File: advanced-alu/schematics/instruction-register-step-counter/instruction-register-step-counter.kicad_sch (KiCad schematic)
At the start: 17 parts, among them SW1 SW_SPST, U1 74LS32, U2 74LS04, U3 74HCT238, U4 74LS161, U5 74LS173, U6 74LS74, U7 74LS173, U8 74LS08

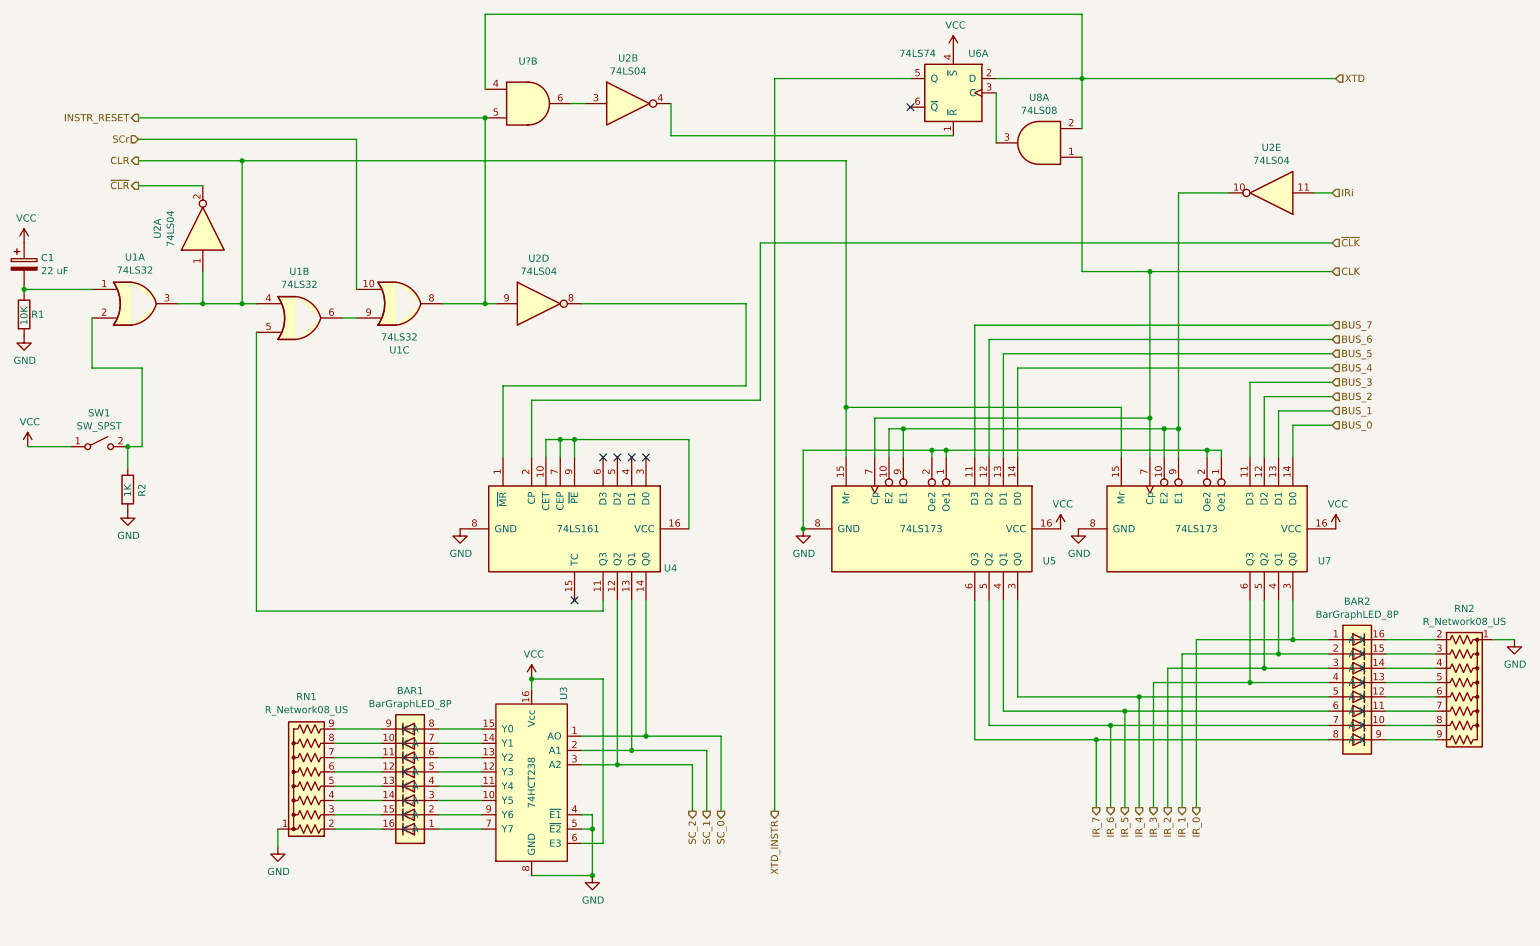
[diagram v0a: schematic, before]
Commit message: fixed STD and step counter resent logic
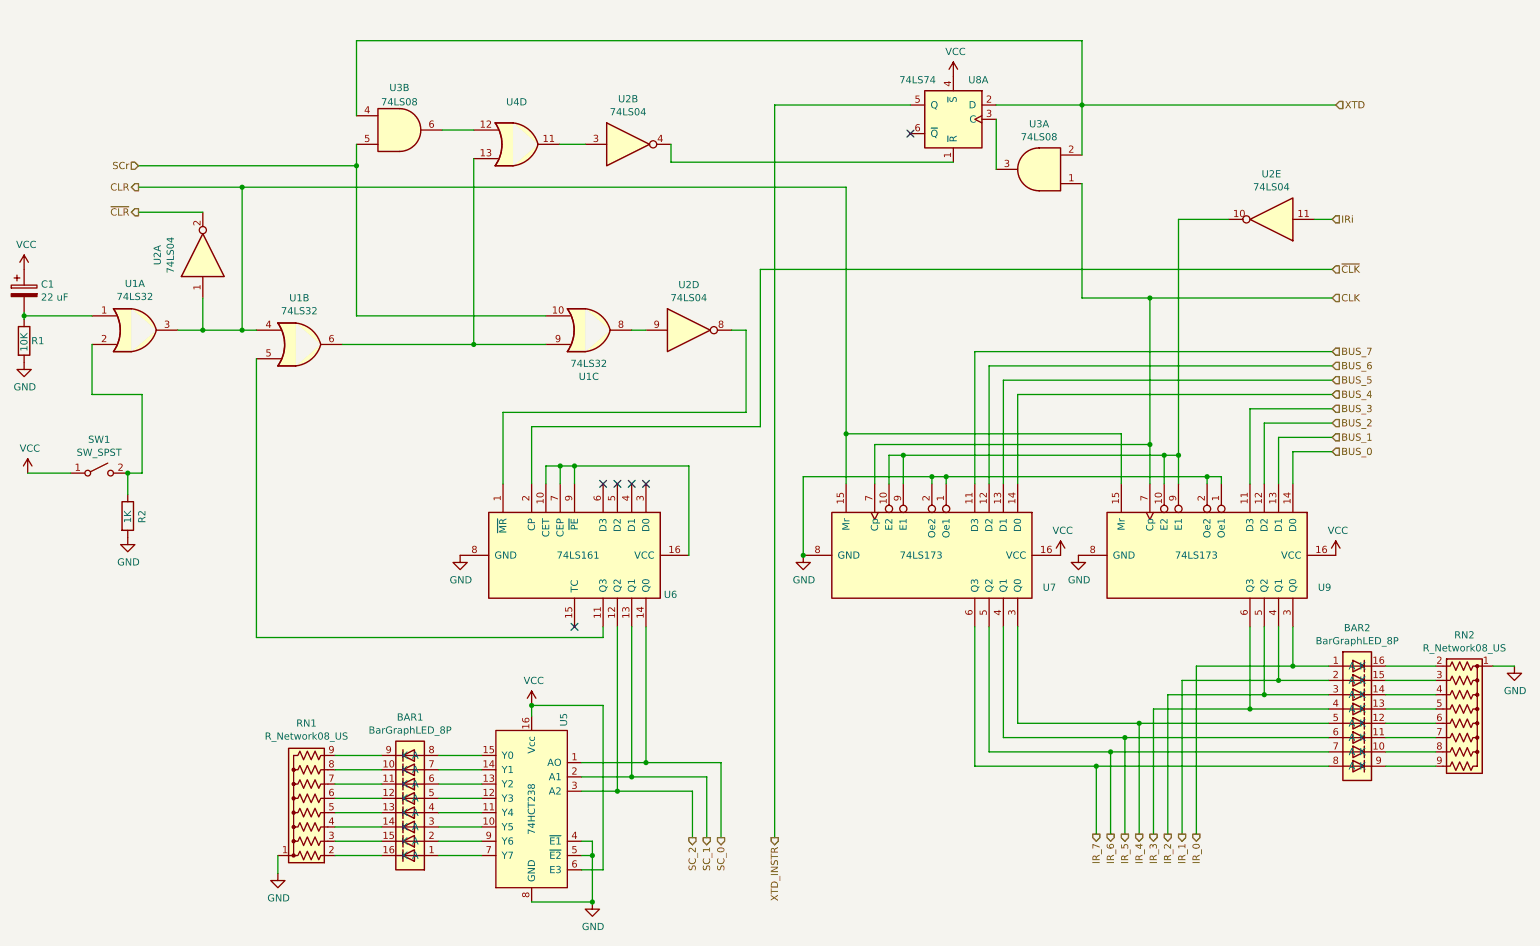
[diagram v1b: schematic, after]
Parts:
- added U4: (no value), symbol 74xx:74LS32
- U3: renamed from U?; value (none) -> 74LS08
- renumbered U8 to U3, U3 to U5, U4 to U6, U5 to U7, U6 to U8, U7 to U9
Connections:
- net SCr: now also U3.5
- net at U1.6, U1.9: now also U4.13
- net at U2.3: now also U4.11; no longer U3.6
- net INSTR_RESET: no longer names the net of U1.8, U2.9
- net INSTR_RESET: no longer U3.5
- new net: U3.6, U4.12
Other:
- moved on the sheet: BAR1, BAR2, C1, R1, R2, RN1, RN2, SW1, U1A, U1B, U1C, U2A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

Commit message: changed how XTD works
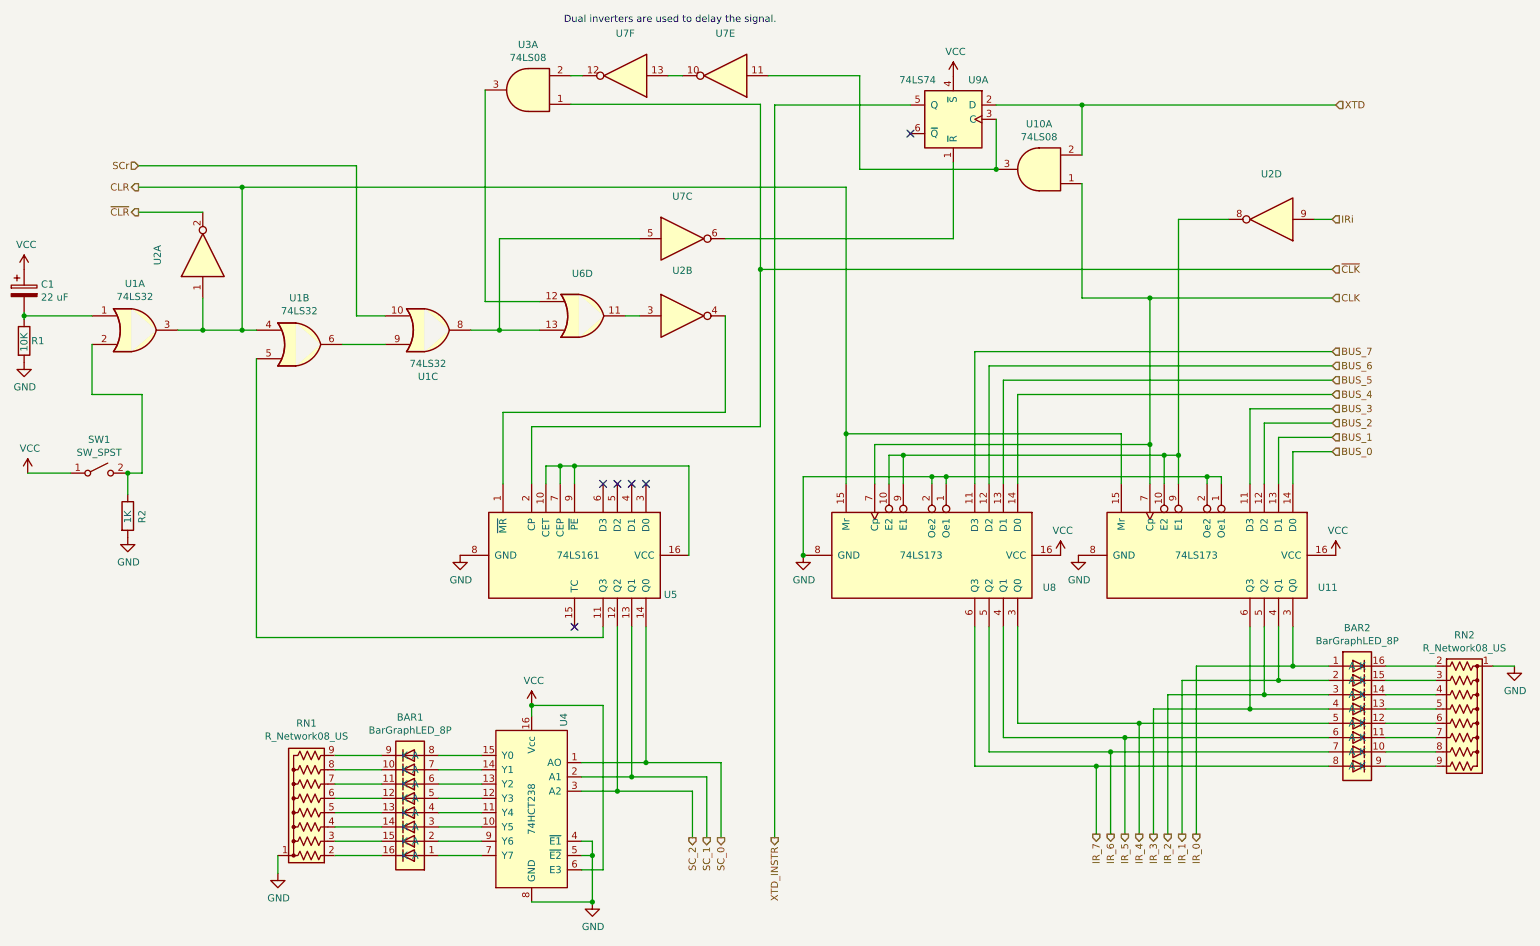
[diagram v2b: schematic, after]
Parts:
- removed unit 2 of U2
- removed unit 2 of U3
- removed U4: (no value), symbol 74xx:74LS32
- added U3: 74LS08, symbol 74xx:74LS08
- added U6: (no value), symbol 74xx:74LS32
- added U7: (no value), symbol 74xx:74LS04
- U2: value 74LS04 -> (none)
- renumbered U3 to U10, U9 to U11, U5 to U4, U6 to U5, U7 to U8, U8 to U9
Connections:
- net IRi: now also U2.9; no longer U2.11
- net ~{CLK}: now also U3.1
- net at U5.1 (~{MR}): now also U2.4; no longer U2.8
- net at U9.1 (~{R}): now also U7.6
- net at U1.8: now also U6.13, U7.5; no longer U2.9
- net at U11.10 (E2), U11.9 (E1), U8.10 (E2)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: now also U2.8; no longer U2.10
- net at U10.3, U9.3 (C): now also U7.11
- new net: U2.3, U6.11
- new net: U3.2, U7.12
- new net: U7.10, U7.13
- new net: U3.3, U6.12
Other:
- note added: "Dual inverters are used to delay the signal."
- moved on the sheet: U1C, U2B

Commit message: updated unit selection
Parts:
- U3: value 74LS08 -> (none)
- U6: value (none) -> 74LS32
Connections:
- net ~{CLK}: now also U3.9; no longer U3.1
- net at U5.1 (~{MR}): now also U2.6; no longer U2.4
- net at U1.8, U6.13: now also U7.9; no longer U7.5
- net at U6.11: now also U2.5; no longer U2.3
- net at U9.1 (~{R}): now also U7.8; no longer U7.6
- net at U10.3, U9.3 (C): now also U7.13; no longer U7.11
- net at U6.12: now also U3.8; no longer U3.3
- new net: U3.10, U7.10
- new net: U7.11, U7.12
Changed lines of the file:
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@@
     (pin "7")
   )
-  (symbol (lib_id "74xx:74LS04") (at 134.112 66.294 0) (unit 2)
+  (symbol (lib_id "74xx:74LS04") (at 134.112 66.294 0) (unit 3)
     (in_bom yes) (on_board yes)
     (property "Reference" "U2" (id 0) (at 134.112 58.2422 0))
@@
     (pin "7")
   )
-  (symbol (lib_id "74xx:74LS04") (at 123.952 23.622 180) (unit 6)
+  (symbol (lib_id "74xx:74LS04") (at 123.952 23.622 180) (unit 5)
     (in_bom yes) (on_board yes) (fields_autoplaced)
     (property "Reference" "U7" (id 0) (at 123.952 16.1122 0))
@@
     (pin "7")
   )
-  (symbol (lib_id "74xx:74LS04") (at 134.112 52.578 0) (unit 3)
+  (symbol (lib_id "74xx:74LS04") (at 134.112 52.578 0) (unit 4)
     (in_bom yes) (on_board yes) (fields_autoplaced)
     (property "Reference" "U7" (id 0) (at 134.112 45.0682 0))
@@
     (pin "7")
   )
-  (symbol (lib_id "74xx:74LS04") (at 141.732 23.622 180) (unit 5)
+  (symbol (lib_id "74xx:74LS04") (at 141.732 23.622 180) (unit 6)
     (in_bom yes) (on_board yes) (fields_autoplaced)
     (property "Reference" "U7" (id 0) (at 141.732 16.1122 0))
@@
     (in_bom yes) (on_board yes) (fields_autoplaced)
     (property "Reference" "U6" (id 0) (at 116.332 58.7842 0))
-    (property "Value" "" (id 1) (at 116.332 61.3211 0))
+    (property "Value" "74LS32" (id 1) (at 116.332 61.3211 0))
     (property "Footprint" "" (id 2) (at 116.332 66.294 0)
       (effects (font (size 1.27 1.27)) hide)
@@
     (pin "7")
   )
-  (symbol (lib_id "74xx:74LS08") (at 106.68 26.162 180) (unit 1)
+  (symbol (lib_id "74xx:74LS08") (at 106.68 26.162 180) (unit 3)
     (in_bom yes) (on_board yes)
     (property "Reference" "U3" (id 0) (at 106.68 18.1102 0))
-    (property "Value" "74LS08" (id 1) (at 106.68 20.4216 0))
+    (property "Value" "" (id 1) (at 106.68 20.4216 0))
     (property "Footprint" "" (id 2) (at 106.68 26.162 0)
       (effects (font (size 1.27 1.27)) hide)
@@
     )
     (path "/00000000-0000-0000-0000-000060d4e826"
-      (reference "U2") (unit 2) (value "74LS04") (footprint "")
+      (reference "U2") (unit 3) (value "74LS04") (footprint "")
     )
     (path "/00000000-0000-0000-0000-000060eae619"
@@
     )
     (path "/c662e862-20c0-4648-89b3-1d6053bef953"
-      (reference "U3") (unit 1) (value "74LS08") (footprint "")
+      (reference "U3") (unit 3) (value "74LS08") (footprint "")
     )
     (path "/00000000-0000-0000-0000-000060d24130"
@@
     )
     (path "/316c4eb7-eb02-4aee-9908-ad637445fc51"
-      (reference "U7") (unit 3) (value "74LS04") (footprint "")
+      (reference "U7") (unit 4) (value "74LS04") (footprint "")
+    )
+    (path "/034761f7-89e6-4cfb-b6ff-bf1b84c7a5df"
+      (reference "U7") (unit 5) (value "74LS04") (footprint "")
     )
     (path "/3c86424c-5cb5-43a6-9f0c-e11641cd17b6"
-      (reference "U7") (unit 5) (value "74LS04") (footprint "")
-    )
-    (path "/034761f7-89e6-4cfb-b6ff-bf1b84c7a5df"
       (reference "U7") (unit 6) (value "74LS04") (footprint "")
     )
